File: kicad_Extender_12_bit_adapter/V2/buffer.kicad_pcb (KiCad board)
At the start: 2 copper layers, 59.9 x 25.7 mm, 8 parts, among them P1 Conn_02x06_Odd_Even, P2 Conn_01x04, P4 Conn_01x08_odd, P5 Conn_01x08_even, P6 Conn_01x01, P7 Conn_01x01

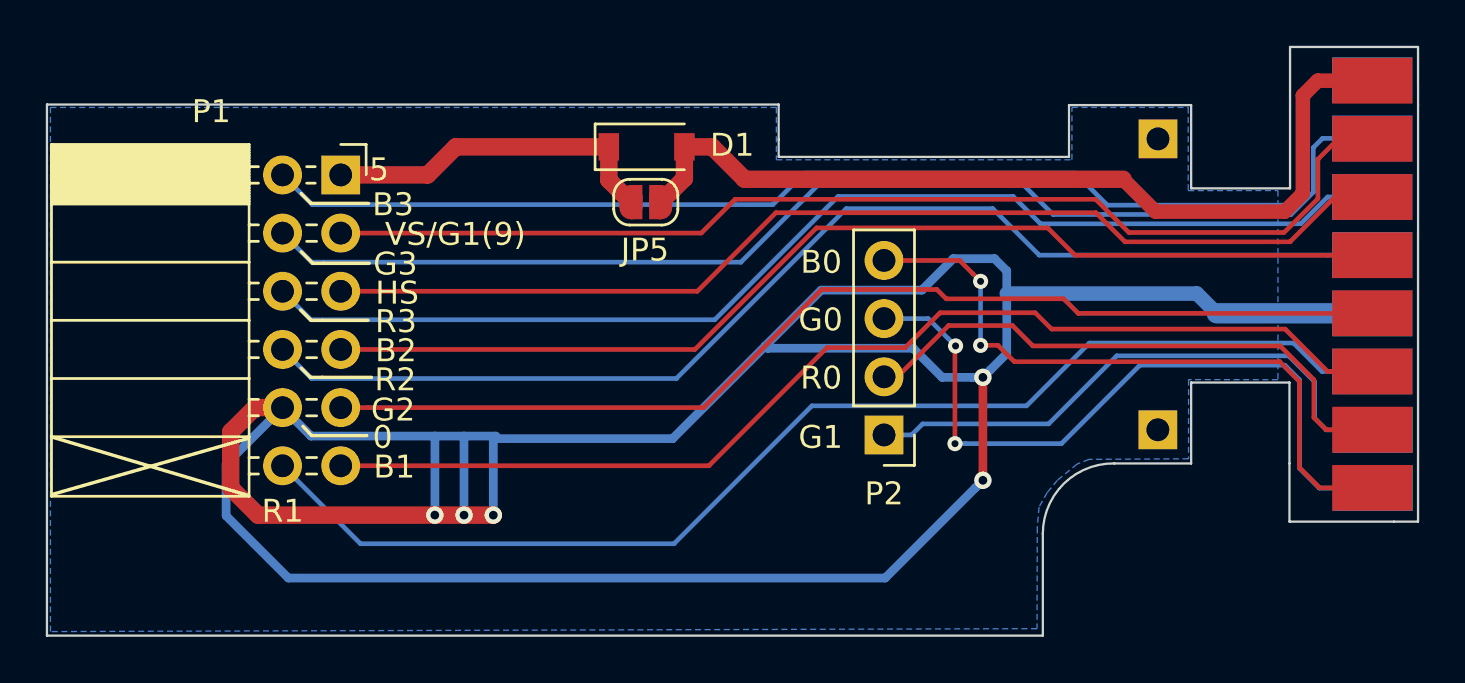
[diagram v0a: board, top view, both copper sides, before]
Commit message: Update 12 bit extender to V2
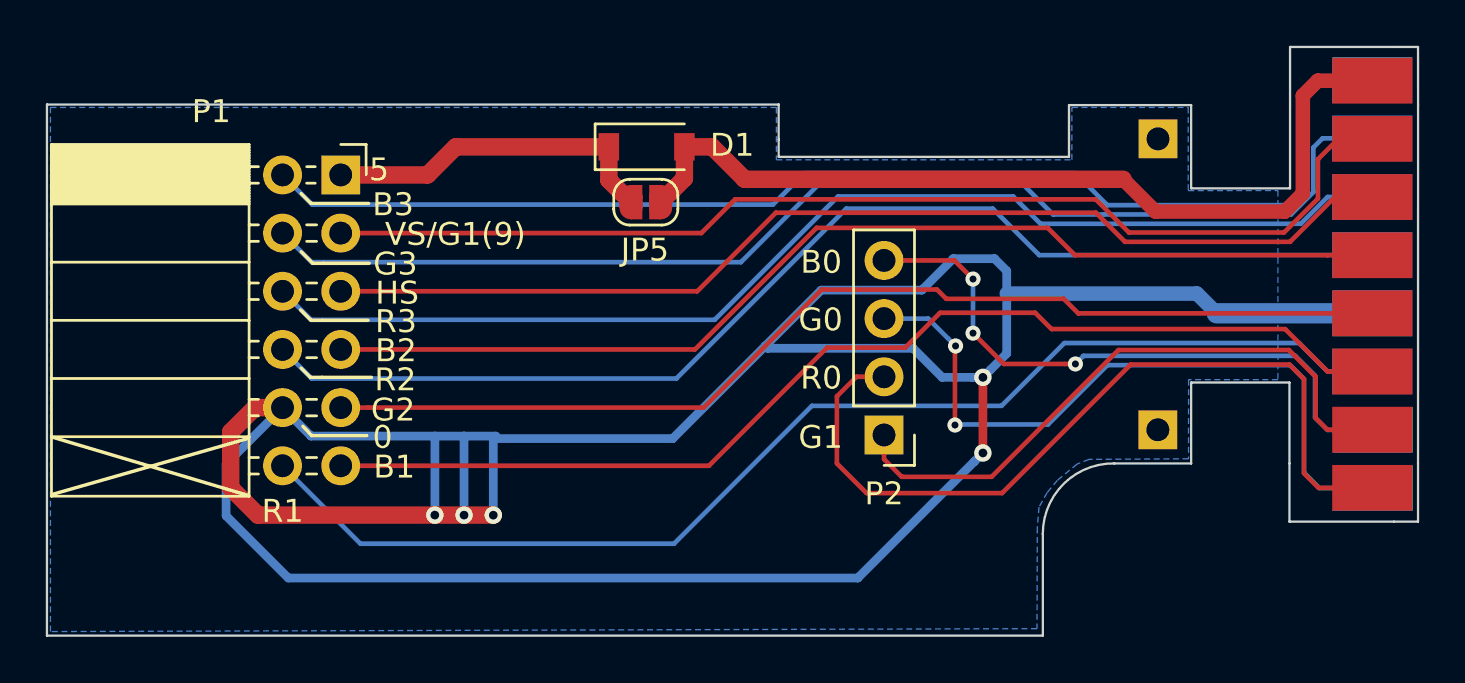
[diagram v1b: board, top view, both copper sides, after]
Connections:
- P4 pad 3: /G1 -> /B0
- P5 pad 2: /B0 -> /R0
- P5 pad 4: /R0 -> /G1
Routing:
- net /R0: track 25.1 -> 36.2 mm
- net /G1: track 25.0 -> 27.5 mm
- net /B0: track 29.3 -> 27.1 mm, vias 2 -> 3
- net /G0: track 32.0 -> 31.0 mm
- net /GND: track 140.9 -> 140.2 mm
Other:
- board text added: "Issue 2 ©2020 IanB"
- board text removed: "Issue 1 ©2020 IanB"
